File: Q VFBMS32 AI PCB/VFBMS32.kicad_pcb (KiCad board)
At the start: 2 copper layers, 130 x 32 mm, 141 parts, among them Q1 AGM15T03LL, Q2 AGM15T03LL, U7 CH340N

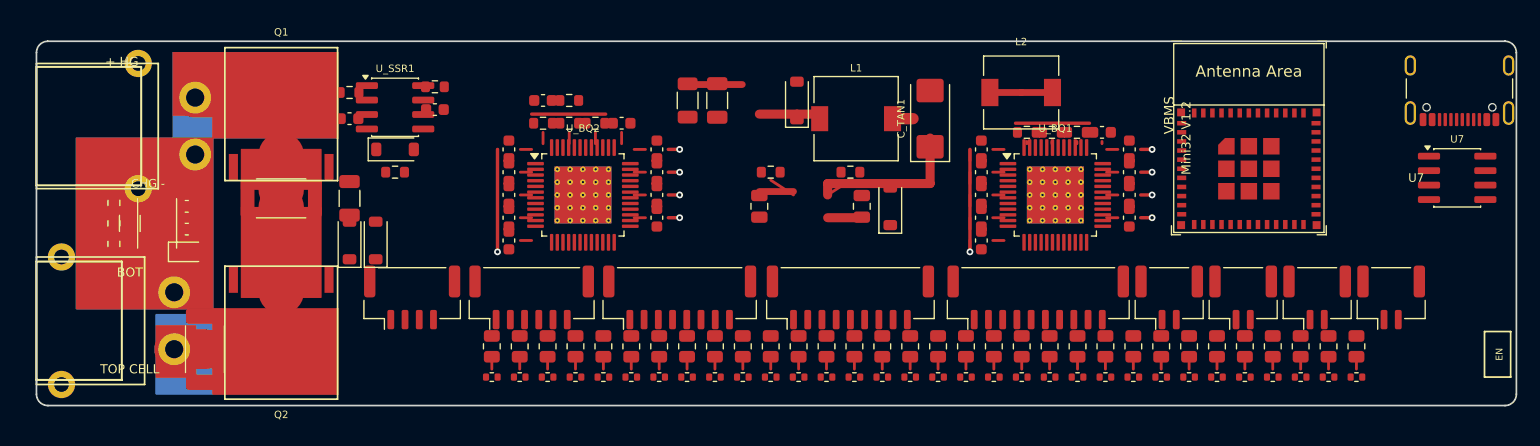
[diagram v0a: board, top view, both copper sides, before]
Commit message: feat: add VFBMS32 AI PCB schematic, layout, and supporting automation scripts
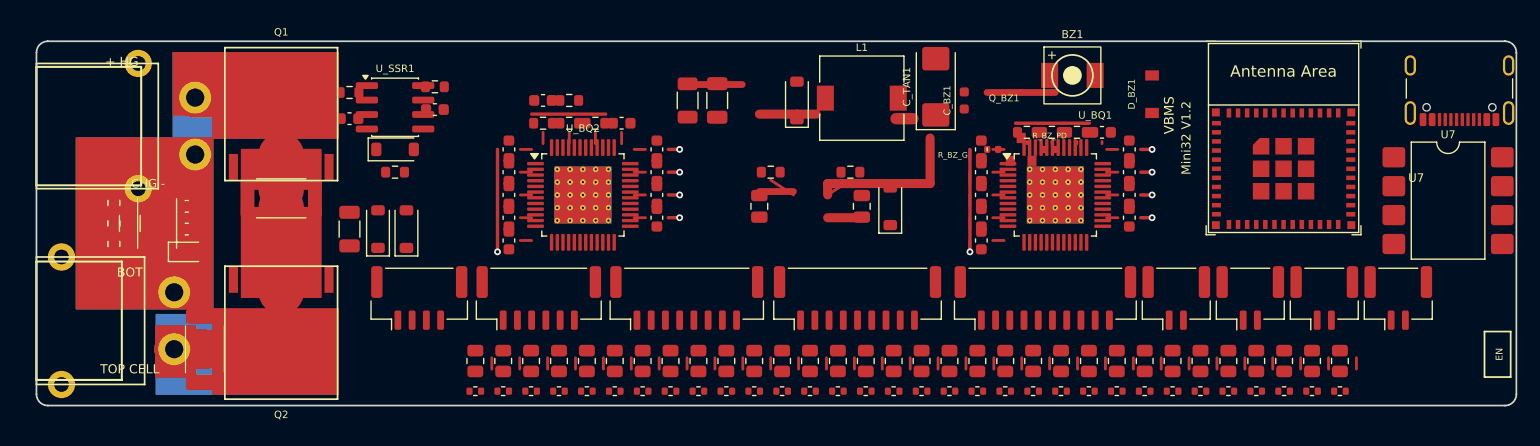
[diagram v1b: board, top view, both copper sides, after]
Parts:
- removed L2: 4.7uH, L_6.3x6.3_H3
- added BZ1: MLT-5030, vfbms:Buzzer_5.0x5.0mm_SMD, F.Cu at (91.0, 3.00)
- added C_BZ1: 1uF, Capacitor_SMD:C_0603_1608Metric, F.Cu at (81.5, 5.20)
- added D_BZ1: B0540W, Diode_SMD:D_SOD-123, F.Cu at (98.0, 4.65)
- added Q_BZ1: 2N7002, Package_TO_SOT_SMD:SOT-23, F.Cu at (86.5, 9.50)
- added R_BZ_G: 100R, Resistor_SMD:R_0402_1005Metric, F.Cu at (84.0, 9.50)
- added R_BZ_PD: 10k, Resistor_SMD:R_0402_1005Metric, F.Cu at (89.0, 9.50)
- U7: value CH340N -> ISO1050 (DUB-8); footprint SOIC-8_3.9x4.9mm_P1.27mm -> Package_DIP:SMDIP-8_W9.53mm
- moved U_ESP1 3.05 mm to (109.5, 8.50)
- moved D_SEC2 2.88 mm to (32.5, 16.5)
- moved C_TAN1 2.84 mm to (79.0, 4.00)
- moved C_DISC 2.70 mm to (27.5, 16.5)
- moved D_SEC1 2.69 mm to (30.0, 16.5)
- moved U7 2.15 mm to (124.0, 14.0)
- moved R_B1 1.94 mm to (38.5, 28.1)
- moved R_B11 1.94 mm to (63.0, 28.1)
- moved R_B12 1.94 mm to (65.5, 28.1)
- moved R_B13 1.94 mm to (68.0, 28.1)
- moved R_B15 1.94 mm to (72.8, 28.1)
- moved R_B16 1.94 mm to (75.3, 28.1)
- moved R_B17 1.94 mm to (77.8, 28.1)
- moved R_B18 1.94 mm to (80.2, 28.1)
- moved R_B2 1.94 mm to (41.0, 28.1)
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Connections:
- U7 pad 1: (no net) -> +3V3
- U7 pad 2: (no net) -> CAN_RX
- U7 pad 3: (no net) -> CAN_TX
- U7 pad 4: (no net) -> GND
- U7 pad 5: (no net) -> ISO_GND
- U7 pad 6: (no net) -> CANL
- U7 pad 7: (no net) -> CANH
- U7 pad 8: (no net) -> 5VExt
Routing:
- net (no net): track 197.1 -> 189.6 mm
- net +3V3: track 0.00 -> 6.50 mm
- net PIN_BUZZER: track 0.00 -> 1.00 mm

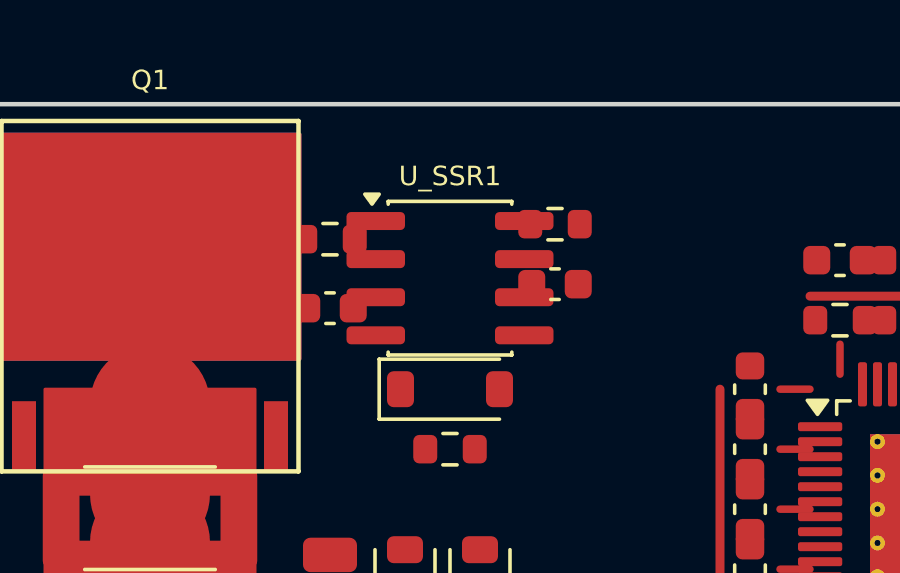
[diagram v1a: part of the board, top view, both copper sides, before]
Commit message: feat: add new KiCad PCB designs and layouts for sf hall ai pcb and Q VFBMS32 AI PCB
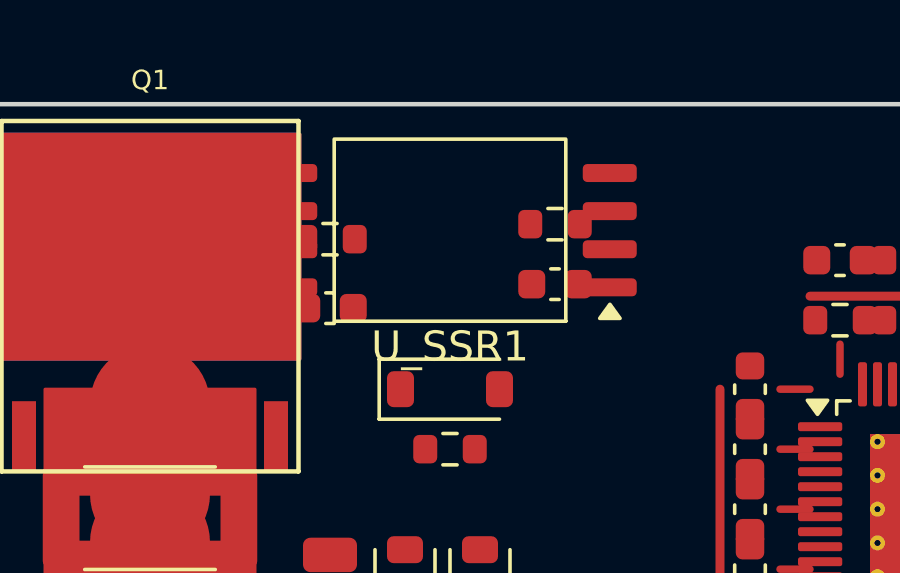
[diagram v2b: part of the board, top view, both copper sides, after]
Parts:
- U_SSR1: value H2440_SSR -> GSRELAY; footprint SOIC-8_3.9x4.9mm_P1.27mm -> SOIC-8_7.5x5.85mm_P1.27mm
- moved U_SSR1 1.60 mm to (31.5, 4.20), turned to 180 degrees

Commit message: fix pcb
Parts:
- moved R_F32 18.2 mm to (96.3, 30.7)
- moved R_B32 18.2 mm to (96.3, 28.1)
- moved R_F31 17.7 mm to (94.4, 30.7)
- moved R_B31 17.6 mm to (94.4, 28.1)
- moved R_F30 17.1 mm to (92.5, 30.7)
- moved R_B30 17.1 mm to (92.5, 28.1)
- moved R_F29 16.6 mm to (90.6, 30.7)
- moved R_B29 16.6 mm to (90.6, 28.1)
- moved R_F28 16.0 mm to (88.7, 30.7)
- moved R_B28 16.0 mm to (88.7, 28.1)
- moved R_F27 15.5 mm to (86.8, 30.7)
- moved R_B27 15.5 mm to (86.8, 28.1)
- moved R_F26 14.9 mm to (84.9, 30.7)
- moved R_B26 14.9 mm to (84.9, 28.1)
- moved R_F25 14.4 mm to (83.0, 30.7)
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
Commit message: feat: add PCB layout project, KiCad bridge, dashboard, and annotator toolset
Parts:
- removed D_V1, D_V2, D_V3: 0603, R_0603_1608Metric
- added D_CHG1: DSK320, D_SOD-123F, F.Cu at (3.15, 15.8)
- added D_CHG2: DSK320, D_SOD-123F, F.Cu at (4.90, 15.8)
- added D_CHG3: DSK320, D_SOD-123F, F.Cu at (6.65, 16.0)
- added R_CHG1: 100k, R_0603_1608Metric, F.Cu at (1.30, 15.8)
- moved F1 26.0 mm to (37.0, 13.5)
- moved Q2 2.90 mm to (24.4, 25.7)
- moved C_S1 2.30 mm to (15.5, 14.5)
- moved D_S1 2.25 mm to (15.4, 18.5)
- moved C_S2 2.03 mm to (15.2, 16.5)
- moved R_SH1 0.90 mm to (11.5, 16.0)
- moved C_FLT1 0.80 mm to (9.00, 16.0)

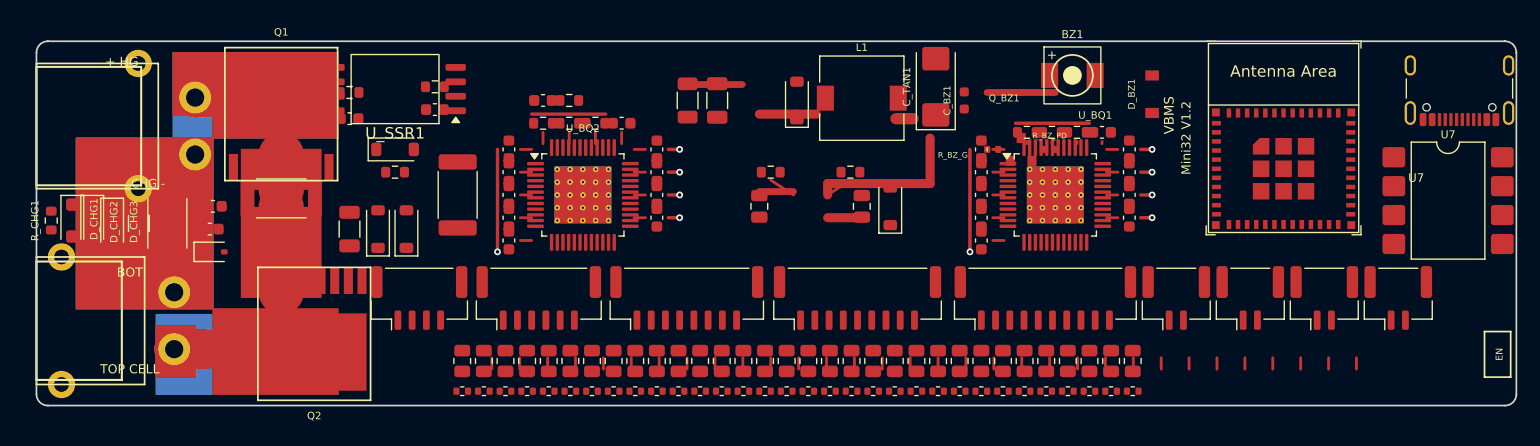
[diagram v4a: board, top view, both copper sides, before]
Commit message: remove  old bad work vfbms  AI PCB
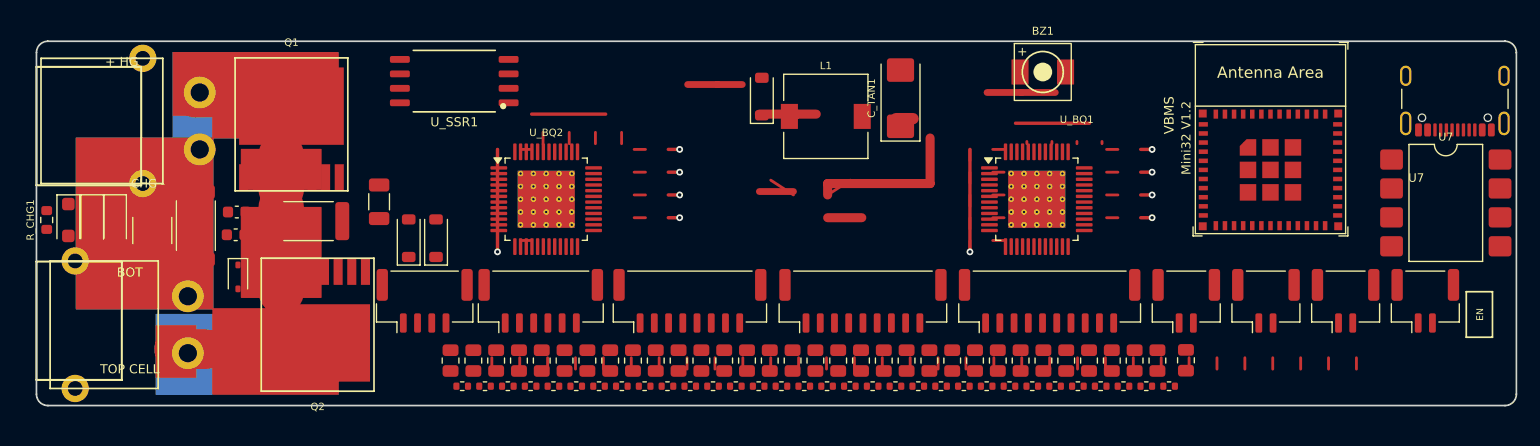
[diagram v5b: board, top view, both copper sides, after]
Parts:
- removed C_BQ1_BAT, C_BQ1_FLT1, C_BQ1_FLT2, C_BQ1_FLT3, C_BQ1_FLT4, C_BQ1_FLT5, C_BQ1_VDD, C_BQ2_BAT, C_BQ2_CP1, C_BQ2_FLT1, C_BQ2_FLT2, C_BQ2_FLT3, C_BQ2_FLT4, C_BQ2_FLT5, C_BQ2_VDD, C_DRV1, C_DRV2: 100nF, C_0603_1608Metric
- removed C_BQ1_REG1, C_BQ1_REG18, C_BQ1_REG2, C_BQ2_REG1, C_BQ2_REG18, C_BQ2_REG2: 2.2uF, C_0603_1608Metric
- removed C_BZ1: 1uF, Capacitor_SMD:C_0603_1608Metric
- removed C_PWR1: 10uF, C_1206_3216Metric
- removed C_PWR2, C_PWR3: 22uF, C_0805_2012Metric
- removed D_BZ1: B0540W, Diode_SMD:D_SOD-123
- removed D_PWR1: Schottky, D_SOD-123
- removed D_TVS1: TVS, D_SOD-123
- removed F1: JT 18A, Fuse_2512_6332Metric
- removed Q_BZ1: 2N7002, Package_TO_SOT_SMD:SOT-23
- removed R_BK_FB1: 100k, R_0603_1608Metric
- removed R_BK_FB2: 22k, R_0603_1608Metric
- removed R_BQ1_PU1, R_BQ1_PU2, R_BQ2_PU1, R_BQ2_PU2: 4k7, R_0603_1608Metric
- removed R_BQ1_PU3, R_BQ2_PU3, R_BQ2_PU4, R_DRV1, R_DRV2: 10k, R_0603_1608Metric
- removed R_BZ_G: 100R, Resistor_SMD:R_0402_1005Metric
- removed R_BZ_PD: 10k, Resistor_SMD:R_0402_1005Metric
- removed R_DRV3: 1k, R_0603_1608Metric
- removed R_PWR1: 10R0, R_1206_3216Metric
- added R_B33: 27R0, R_0805_2012Metric, F.Cu at (101.0, 28.0)
- BZ1: value MLT-5030 -> Buzzer
- C_FLT1: footprint C_1206_3216Metric -> C_1812_4532Metric
- U_SSR1: footprint SOIC-8_7.5x5.85mm_P1.27mm -> vfbms:H2440_SSR
- moved U_SSR1 5.25 mm to (36.7, 3.50)
- moved D_SEC1 5.16 mm to (35.1, 17.3)
- moved L1 3.54 mm to (69.3, 6.60)
- moved C_DISC 3.54 mm to (30.1, 14.1)
- moved C_TAN1 3.26 mm to (75.9, 5.00)
- moved U_BQ2 3.25 mm to (44.8, 13.9)
- moved R_F32 3.22 mm to (99.5, 30.3)
- moved D_S1 3.15 mm to (17.7, 20.7), turned to -90 degrees
- moved R_SH2 3.12 mm to (23.9, 15.8)
- moved R_F31 3.12 mm to (97.5, 30.3)
- moved D_BST1 3.10 mm to (63.7, 4.86)
- moved R_F30 3.02 mm to (95.5, 30.3)
- moved R_F29 2.92 mm to (93.5, 30.3)
- moved R_F28 2.82 mm to (91.5, 30.3)
- moved R_F27 2.71 mm to (89.5, 30.3)
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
